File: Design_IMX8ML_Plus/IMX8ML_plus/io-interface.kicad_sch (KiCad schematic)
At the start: 1 part, among them U1 MIMX8ML8CVNKZAB

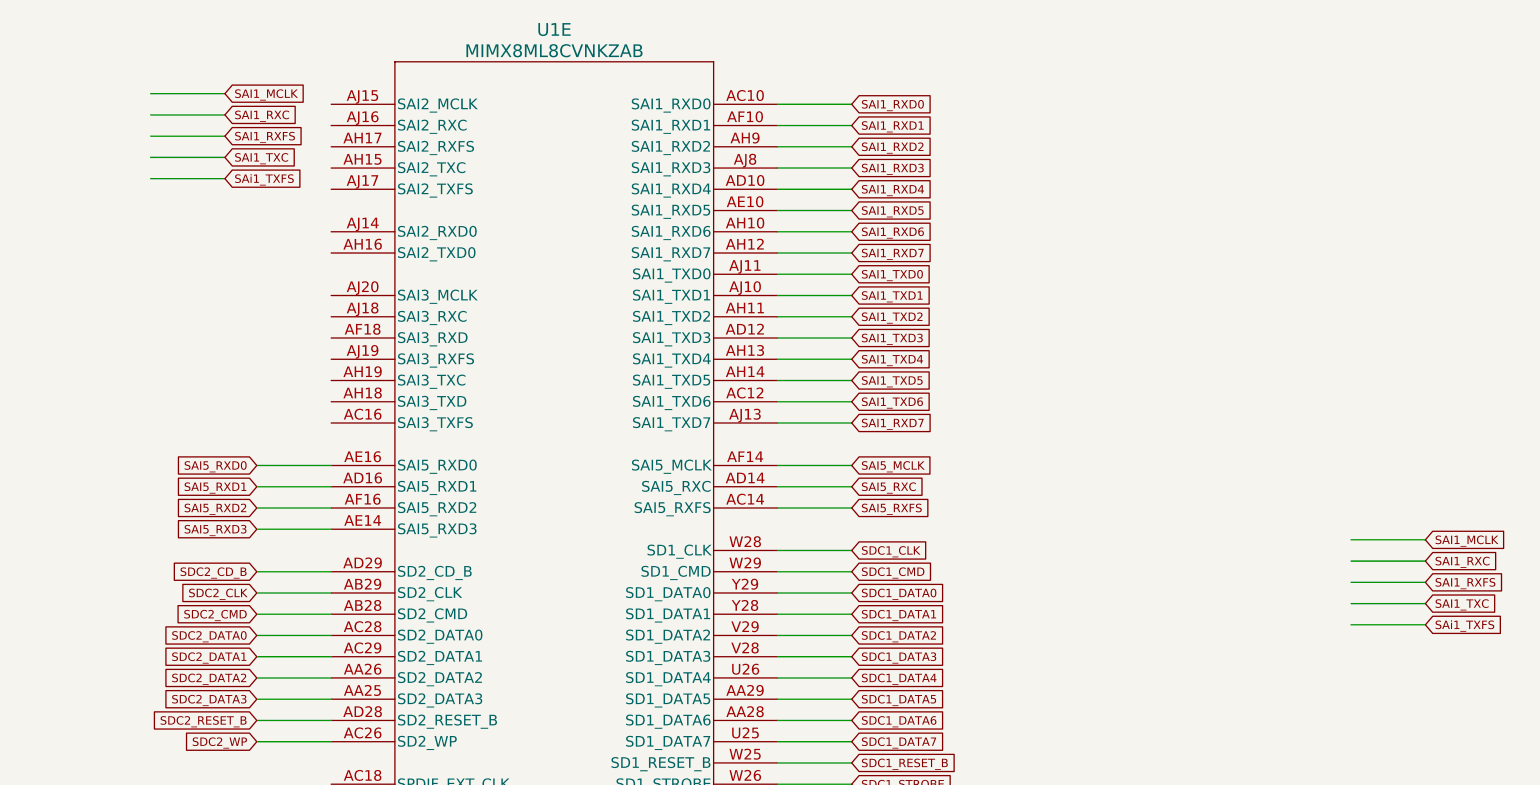
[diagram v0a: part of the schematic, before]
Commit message: processor capacitors location
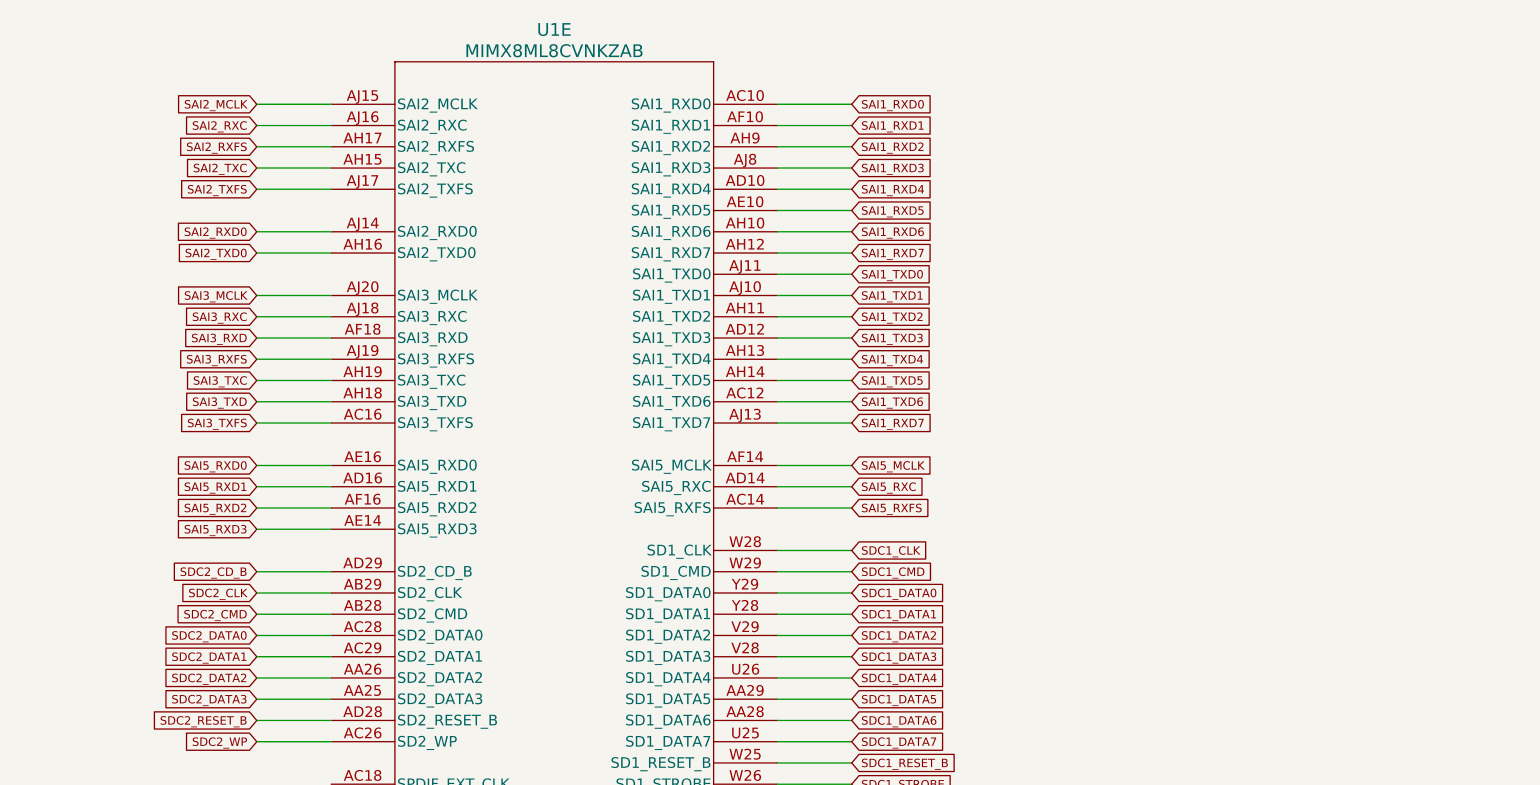
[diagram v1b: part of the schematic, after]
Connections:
- net SAI3_TXFS: now reaches U1.AC16 (SAI3_TXFS)
- net SAI3_RXD: now reaches U1.AF18 (SAI3_RXD)
- net SAI2_TXC: now reaches U1.AH15 (SAI2_TXC)
- net SAI2_TXD0: now reaches U1.AH16 (SAI2_TXD0)
- net SAI2_RXFS: now reaches U1.AH17 (SAI2_RXFS)
- net SAI3_TXD: now reaches U1.AH18 (SAI3_TXD)
- net SAI3_TXC: now reaches U1.AH19 (SAI3_TXC)
- net SAI2_RXD0: now reaches U1.AJ14 (SAI2_RXD0)
- net SAI2_MCLK: now reaches U1.AJ15 (SAI2_MCLK)
- net SAI2_RXC: now reaches U1.AJ16 (SAI2_RXC)
- net SAI2_TXFS: now reaches U1.AJ17 (SAI2_TXFS)
- net SAI3_RXC: now reaches U1.AJ18 (SAI3_RXC)
- net SAI3_RXFS: now reaches U1.AJ19 (SAI3_RXFS)
- net SAI3_MCLK: now reaches U1.AJ20 (SAI3_MCLK)

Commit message: Update schematic and add ethernet interface ksz9131rn
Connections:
- net HDM_CEC renamed HDMI_CEC
- net HDM_DDC_SCL renamed HDMI_DDC_SCL
- net HDM_DDC_SDA renamed HDMI_DDC_SDA
- net HDM_HPD renamed HDMI_HPD
- net HDM_TX0_N renamed HDMI_TX0_N
- net HDM_TX0_P renamed HDMI_TX0_P
- net HDM_TX1_N renamed HDMI_TX1_N
- net HDM_TX1_P renamed HDMI_TX1_P
- net HDM_TX2_N renamed HDMI_TX2_N
- net HDM_TX2_P renamed HDMI_TX2_P
- net HDM_TXC_N renamed HDMI_TXC_N
- net HDM_TXC_P renamed HDMI_TXC_P
- net USB1_BUS renamed USB1_VBUS
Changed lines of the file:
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@@
     )
   )
-  (global_label "HDM_TX0_N" (shape input) (at 34.29 72.39 180) (fields_autoplaced)
-    (effects (font (size 1 1)) (justify right))
-    (property "Intersheetrefs" "${INTERSHEET_REFS}" (at 23.5735 72.39 0)
+  (global_label "HDMI_TX0_N" (shape input) (at 34.29 72.39 180) (fields_autoplaced)
+    (effects (font (size 1 1)) (justify right))
+    (property "Intersheetrefs" "${INTERSHEET_REFS}" (at 23.0973 72.39 0)
       (effects (font (size 1.27 1.27)) (justify right) hide)
     )
@@
     )
   )
-  (global_label "HDM_DDC_SCL" (shape input) (at 34.29 62.23 180) (fields_autoplaced)
-    (effects (font (size 1 1)) (justify right))
-    (property "Intersheetrefs" "${INTERSHEET_REFS}" (at 21.5259 62.23 0)
+  (global_label "HDMI_DDC_SCL" (shape input) (at 34.29 62.23 180) (fields_autoplaced)
+    (effects (font (size 1 1)) (justify right))
+    (property "Intersheetrefs" "${INTERSHEET_REFS}" (at 21.0497 62.23 0)
       (effects (font (size 1.27 1.27)) (justify right) hide)
     )
@@
     )
   )
-  (global_label "HDM_CEC" (shape input) (at 34.29 59.69 180) (fields_autoplaced)
-    (effects (font (size 1 1)) (justify right))
-    (property "Intersheetrefs" "${INTERSHEET_REFS}" (at 25.1449 59.69 0)
+  (global_label "HDMI_CEC" (shape input) (at 34.29 59.69 180) (fields_autoplaced)
+    (effects (font (size 1 1)) (justify right))
+    (property "Intersheetrefs" "${INTERSHEET_REFS}" (at 24.6687 59.69 0)
       (effects (font (size 1.27 1.27)) (justify right) hide)
     )
@@
     )
   )
-  (global_label "HDM_TXC_P" (shape input) (at 34.29 90.17 180) (fields_autoplaced)
-    (effects (font (size 1 1)) (justify right))
-    (property "Intersheetrefs" "${INTERSHEET_REFS}" (at 23.5735 90.17 0)
+  (global_label "HDMI_TXC_P" (shape input) (at 34.29 90.17 180) (fields_autoplaced)
+    (effects (font (size 1 1)) (justify right))
+    (property "Intersheetrefs" "${INTERSHEET_REFS}" (at 23.0973 90.17 0)
       (effects (font (size 1.27 1.27)) (justify right) hide)
     )
@@
     )
   )
-  (global_label "HDM_TX0_P" (shape input) (at 34.29 74.93 180) (fields_autoplaced)
-    (effects (font (size 1 1)) (justify right))
-    (property "Intersheetrefs" "${INTERSHEET_REFS}" (at 23.6211 74.93 0)
+  (global_label "HDMI_TX0_P" (shape input) (at 34.29 74.93 180) (fields_autoplaced)
+    (effects (font (size 1 1)) (justify right))
+    (property "Intersheetrefs" "${INTERSHEET_REFS}" (at 23.1449 74.93 0)
       (effects (font (size 1.27 1.27)) (justify right) hide)
     )
@@
     )
   )
-  (global_label "HDM_TX1_P" (shape input) (at 34.29 80.01 180) (fields_autoplaced)
-    (effects (font (size 1 1)) (justify right))
-    (property "Intersheetrefs" "${INTERSHEET_REFS}" (at 23.6211 80.01 0)
+  (global_label "HDMI_TX1_P" (shape input) (at 34.29 80.01 180) (fields_autoplaced)
+    (effects (font (size 1 1)) (justify right))
+    (property "Intersheetrefs" "${INTERSHEET_REFS}" (at 23.1449 80.01 0)
       (effects (font (size 1.27 1.27)) (justify right) hide)
     )
@@
     )
   )
-  (global_label "HDM_TX2_P" (shape input) (at 34.29 85.09 180) (fields_autoplaced)
-    (effects (font (size 1 1)) (justify right))
-    (property "Intersheetrefs" "${INTERSHEET_REFS}" (at 23.6211 85.09 0)
+  (global_label "HDMI_TX2_P" (shape input) (at 34.29 85.09 180) (fields_autoplaced)
+    (effects (font (size 1 1)) (justify right))
+    (property "Intersheetrefs" "${INTERSHEET_REFS}" (at 23.1449 85.09 0)
       (effects (font (size 1.27 1.27)) (justify right) hide)
     )
@@
     )
   )
-  (global_label "USB1_BUS" (shape input) (at 167.64 142.24 180) (fields_autoplaced)
-    (effects (font (size 1 1)) (justify right))
-    (property "Intersheetrefs" "${INTERSHEET_REFS}" (at 157.6378 142.24 0)
+  (global_label "USB1_VBUS" (shape input) (at 167.64 142.24 180) (fields_autoplaced)
+    (effects (font (size 1 1)) (justify right))
+    (property "Intersheetrefs" "${INTERSHEET_REFS}" (at 156.7807 142.24 0)
       (effects (font (size 1.27 1.27)) (justify right) hide)
     )
@@
     )
   )
-  (global_label "HDM_TX2_N" (shape input) (at 34.29 82.55 180) (fields_autoplaced)
-    (effects (font (size 1 1)) (justify right))
-    (property "Intersheetrefs" "${INTERSHEET_REFS}" (at 23.5735 82.55 0)
-      (effects (font (size 1.27 1.27)) (justify right) hide)
-    )
-  )
-  (global_label "HDM_TXC_N" (shape input) (at 34.29 87.63 180) (fields_autoplaced)
-    (effects (font (size 1 1)) (justify right))
-    (property "Intersheetrefs" "${INTERSHEET_REFS}" (at 23.5259 87.63 0)
+  (global_label "HDMI_TX2_N" (shape input) (at 34.29 82.55 180) (fields_autoplaced)
+    (effects (font (size 1 1)) (justify right))
+    (property "Intersheetrefs" "${INTERSHEET_REFS}" (at 23.0973 82.55 0)
+      (effects (font (size 1.27 1.27)) (justify right) hide)
+    )
+  )
+  (global_label "HDMI_TXC_N" (shape input) (at 34.29 87.63 180) (fields_autoplaced)
+    (effects (font (size 1 1)) (justify right))
+    (property "Intersheetrefs" "${INTERSHEET_REFS}" (at 23.0497 87.63 0)
       (effects (font (size 1.27 1.27)) (justify right) hide)
     )
@@
     )
   )
-  (global_label "HDM_HPD" (shape input) (at 34.29 67.31 180) (fields_autoplaced)
-    (effects (font (size 1 1)) (justify right))
-    (property "Intersheetrefs" "${INTERSHEET_REFS}" (at 25.0021 67.31 0)
+  (global_label "HDMI_HPD" (shape input) (at 34.29 67.31 180) (fields_autoplaced)
+    (effects (font (size 1 1)) (justify right))
+    (property "Intersheetrefs" "${INTERSHEET_REFS}" (at 24.5259 67.31 0)
       (effects (font (size 1.27 1.27)) (justify right) hide)
     )
@@
     )
   )
-  (global_label "HDM_DDC_SDA" (shape input) (at 34.29 64.77 180) (fields_autoplaced)
-    (effects (font (size 1 1)) (justify right))
-    (property "Intersheetrefs" "${INTERSHEET_REFS}" (at 21.4783 64.77 0)
+  (global_label "HDMI_DDC_SDA" (shape input) (at 34.29 64.77 180) (fields_autoplaced)
+    (effects (font (size 1 1)) (justify right))
+    (property "Intersheetrefs" "${INTERSHEET_REFS}" (at 21.0021 64.77 0)
       (effects (font (size 1.27 1.27)) (justify right) hide)
     )
@@
     )
   )
-  (global_label "HDM_TX1_N" (shape input) (at 34.29 77.47 180) (fields_autoplaced)
-    (effects (font (size 1 1)) (justify right))
-    (property "Intersheetrefs" "${INTERSHEET_REFS}" (at 23.5735 77.47 0)
-      (effects (font (size 1.27 1.27)) (justify right) hide)
-    )
+  (global_label "HDMI_TX1_N" (shape input) (at 34.29 77.47 180) (fields_autoplaced)
+    (effects (font (size 1 1)) (justify right))
+    (property "Intersheetrefs" "${INTERSHEET_REFS}" (at 23.0973 77.47 0)
+      (effects (font (size 1.27 1.27)) (justify right) hide)
+    )

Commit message: CPU Board actualizate
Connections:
- net USB1_DNU: now reaches U1.B11 (USB1_DNU)
- net USB1_TXRTUNE: now reaches U1.F10 (USB1_TXRTUNE)
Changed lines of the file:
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@@
 	(wire
 		(pts
+			(xy 176.53 139.7) (xy 167.64 139.7)
+		)
+		(stroke
+			(width 0)
+			(type default)
+		)
+	)
+	(wire
+		(pts
 			(xy 43.18 41.91) (xy 34.29 41.91)
 		)
@@
 	(wire
 		(pts
+			(xy 176.53 127) (xy 167.64 127)
+		)
+		(stroke
+			(width 0)
+			(type default)
+		)
+	)
+	(wire
+		(pts
 			(xy 176.53 134.62) (xy 167.64 134.62)
 		)
@@
 		)
 	)
+	(global_label "USB1_TXRTUNE"
+		(shape input)
+		(at 167.64 139.7 180)
+		(fields_autoplaced yes)
+		(effects
+			(font
+				(size 1 1)
+			)
+			(justify right)
+		)
+		(property "Intersheetrefs" "${INTERSHEET_REFS}"
+			(at 154.0992 139.7 0)
+			(effects
+				(font
+					(size 1.27 1.27)
+				)
+				(justify right)
+				(hide yes)
+			)
+		)
+	)
 	(global_label "LVDS0_D1_N"
 		(shape input)
@@
 				(hide yes)
 			)
+		)
+	)
+	(global_label "USB1_DNU"
+		(shape input)
+		(at 167.64 127 180)
+		(fields_autoplaced yes)
+		(effects
+			(font
+				(size 1 1)
+			)
+			(justify right)
+		)
+		(property "Intersheetrefs" "${INTERSHEET_REFS}"
+			(at 157.4802 127 0)
+			(effects
+				(font
+					(size 1.27 1.27)
+				)
+				(justify right)
+				(hide yes)
+			)

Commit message: [PROCESSOR] Create zones It added power zones in the four layer
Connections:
- net SAI1_RXD7: no longer U1.AJ13 (SAI1_TXD7)
- net SAI2_TXFS renamed SAI_2_TXFS
- new net SAI1_TXD7: U1.AJ13 (SAI1_TXD7)
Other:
- note added: "CAN1_RX"
- note added: "CAN1_TX"
- note added: "CAN2_RX"
- note added: "CAN2_TX"
- note added: "CSI_1_MCLK"
- note added: "CTRL_SLEEP_MOCI#"
- note added: "ETH_2_RGMII_INT#"
- note added: "ETH_2_RGMII_MDC"
- note added: "ETH_2_RGMII_MDIO"
- note added: "ETH_2_RGMII_RXD_0"
- note added: "ETH_2_RGMII_RXD_1"
- note added: "ETH_2_RGMII_RXD_2"
- note added: "ETH_2_RGMII_RXD_3"
- note added: "ETH_2_RGMII_TXD_0"
- note added: "ETH_2_RGMII_TXD_1"
- note added: "ETH_2_RGMII_TXD_2"
- note added: "ETH_2_RGMII_TXD_3"
- note added: "ETH_2_RGMII_TX_CTL"
- note added: "ETH_2_RGMII_TX_TXC"
- note added: "GPIO_10_DSI"
- note added: "GPIO_5_CSI"
- note added: "GPIO_6_CSI"
- note added: "GPIO_7_CSI"
- note added: "GPIO_9_DSI"
- note added: "I2S_1_BCLK"
- note added: "I2S_1_D_IN"
- note added: "I2S_1_D_OUT"
- note added: "I2S_1_SYNC"
- note added: "I2S_2_BCLK"
- note added: "I2S_2_D_IN"
- note added: "I2S_2_D_OUT"
- note added: "I2S_2_SYNC"
- note added: "PCIe_1_RESET#"
- note added: "PWM_2"
- note added: "PWM_3_DSI"
- note added: "SD1_PWR_EN"
- note added: "UART_1_CTS"
- note added: "UART_1_RTS"
- note added: "USB_1_EN"
- note added: "USB_1_ID"
- note added: "USB_1_OC#"
- note added: "USB_2_EN"
- note added: "UsB_2_OC#"
